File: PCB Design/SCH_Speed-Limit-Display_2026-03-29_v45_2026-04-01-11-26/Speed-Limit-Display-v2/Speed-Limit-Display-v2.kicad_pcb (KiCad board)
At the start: 2 copper layers, 75 x 58.5 mm, 28 parts, among them J1 USB_C_Receptacle, J2 Conn_01x12_Pin, J3 Conn_Coaxial, SW1 RotaryEncoder_Switch, SW3 SW_Push, SW4 SW_Push, U1 ESP32-S3-WROOM-1, U2 L70-R, U3 TLV75530PDBV, U4 USBLC6-2P6

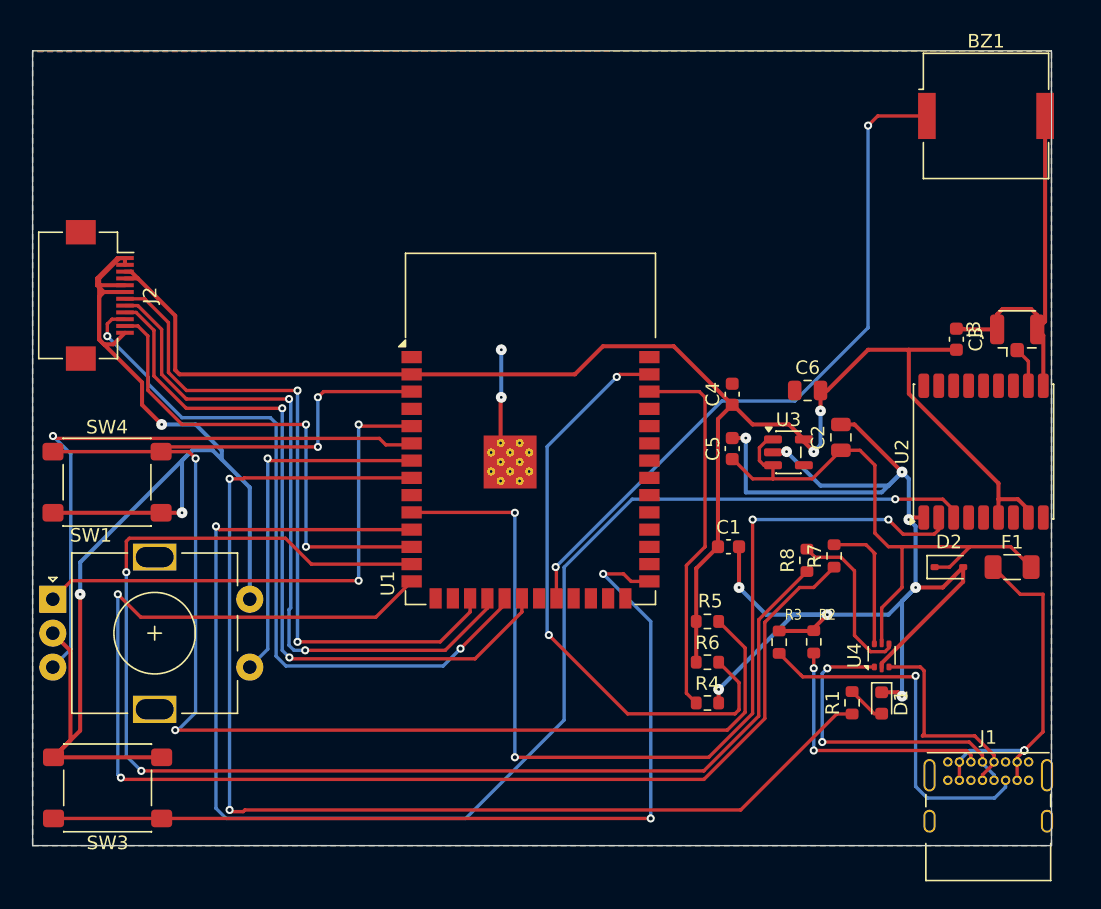
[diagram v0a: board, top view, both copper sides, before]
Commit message: feat: add J4 breakout header, Gerber/ordering docs, final DRC clean
Added 9-pin breakout header (J4) exposing IO35, IO36, IO45, IO46,
TXD0, RXD0, +3V3, +5V, GND for future sensor expansion. Updated
PCB design docs with step-by-step Gerber generation instructions,
PCBWay/JLCPCB ordering guide, component sourcing, and assembly notes.
Final DRC: 0 errors, 2 cosmetic silkscreen warnings only.

Co-Authored-By: Claude Opus 4.6 (1M context) <noreply@anthropic.com>
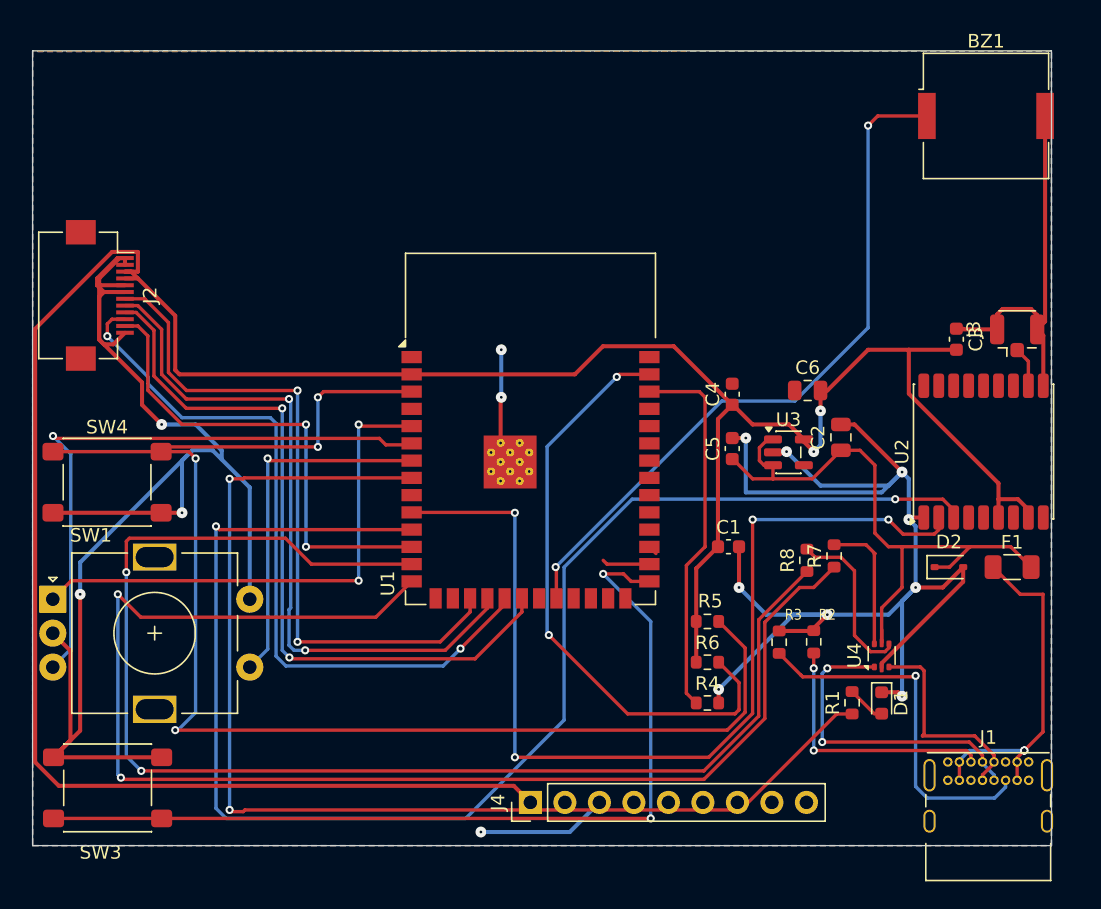
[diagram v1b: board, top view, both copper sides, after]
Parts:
- added J4: Conn_01x09_Pin, Connector_PinHeader_2.54mm:PinHeader_1x09_P2.54mm_Vertical, F.Cu at (79.1, 95.8)
- R7, R8: value 22 -> R
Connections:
- U1 pad 16: unconnected-(U1-IO46-Pad16) -> /IO46
- U1 pad 26: unconnected-(U1-IO45-Pad26) -> /IO45
- U1 pad 28: unconnected-(U1-IO35-Pad28) -> /IO35
- U1 pad 29: unconnected-(U1-IO36-Pad29) -> /IO36
- U1 pad 36: unconnected-(U1-RXD0-Pad36) -> /RXD0
- U1 pad 37: unconnected-(U1-TXD0-Pad37) -> /TXD0
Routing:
- net +3V3: track 115.5 -> 197.4 mm
- net GND: track 245.5 -> 255.1 mm, vias 14 -> 15
- net /IO35: track 0.00 -> 3.52 mm
- net +5V: track 45.2 -> 46.2 mm
- net /IO36: track 0.00 -> 0.69 mm

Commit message: feat: add Gerber files, update README and product plan
Added zipped Gerber + drill files ready for PCBWay/JLCPCB upload.
Updated README with custom PCB section and full project structure.
Updated product plan: Phase 3 PCB Design marked as nearly complete
(5/6 tasks done, only board ordering remains).

Co-Authored-By: Claude Opus 4.6 (1M context) <noreply@anthropic.com>
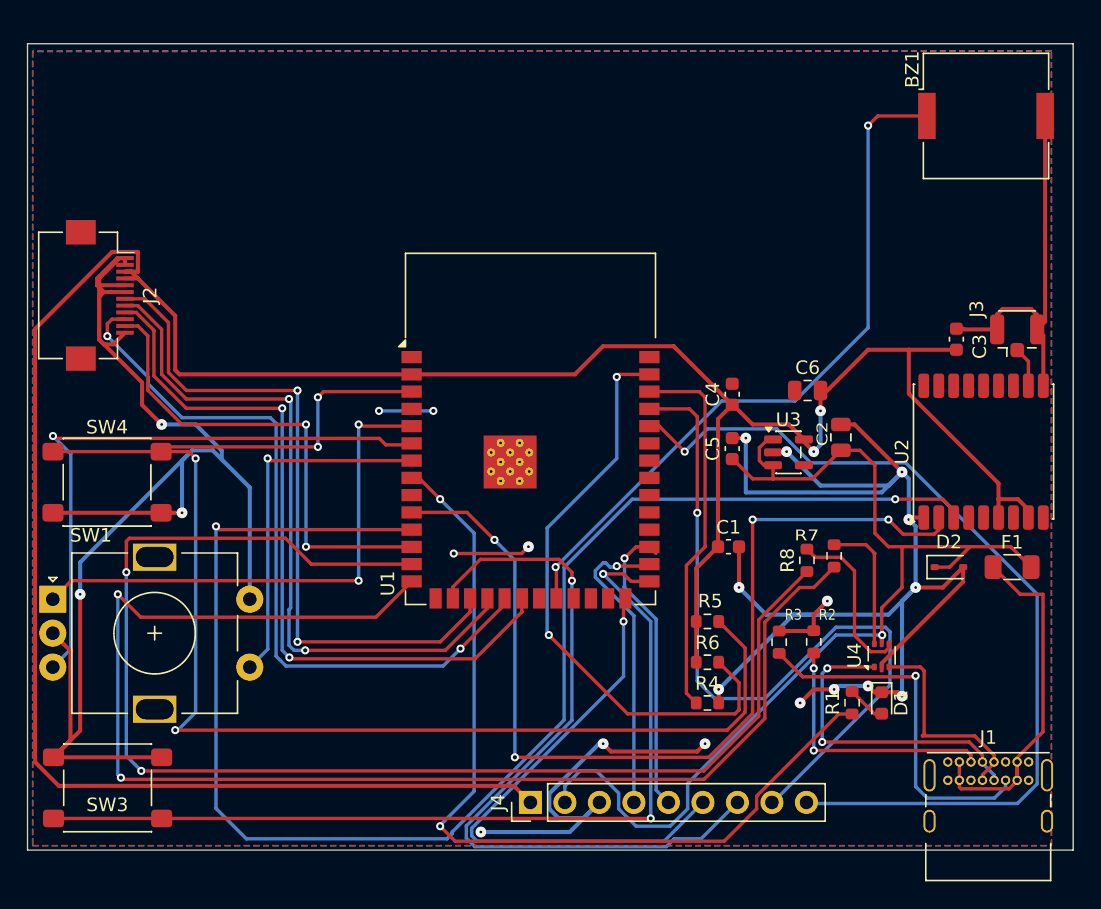
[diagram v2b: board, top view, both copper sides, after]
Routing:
- net /RXD0: track 0.00 -> 66.6 mm, vias 0 -> 1
- net /TXD0: track 0.00 -> 57.1 mm, vias 0 -> 1
- net /IO46: track 0.00 -> 55.2 mm, vias 0 -> 1
- net /IO45: track 0.00 -> 40.5 mm, vias 0 -> 1
- net +5V: track 46.2 -> 81.1 mm, vias 0 -> 1
- net GND: track 255.1 -> 284.7 mm, vias 15 -> 22
- net Net-(U1-IO15): track 86.8 -> 64.7 mm
- net /IO36: track 0.69 -> 22.2 mm, vias 0 -> 1
- net /IO35: track 3.52 -> 22.7 mm, vias 0 -> 1
- net Net-(U1-IO17): track 73.9 -> 71.9 mm
- net Net-(F1-Pad1): track 25.5 -> 26.9 mm, vias 2 -> 0
- net Net-(U1-IO18): track 107.6 -> 108.9 mm
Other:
- board size 75 x 58.5 mm -> 77 x 59.4 mm
